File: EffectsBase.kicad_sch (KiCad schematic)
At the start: 17 parts, among them J1 PCIE_FX, J2 Conn_01x02, J3 Conn_01x02, K2 G6K-2, SW1 SW_DPDT_x2, SW2 SW_DPDT_x2, SW3 SW_DPDT_x2, SW4 SW_DPDT_x2, U1 STM32F103C8Tx, X1 PEDAL_COMBO_TOP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

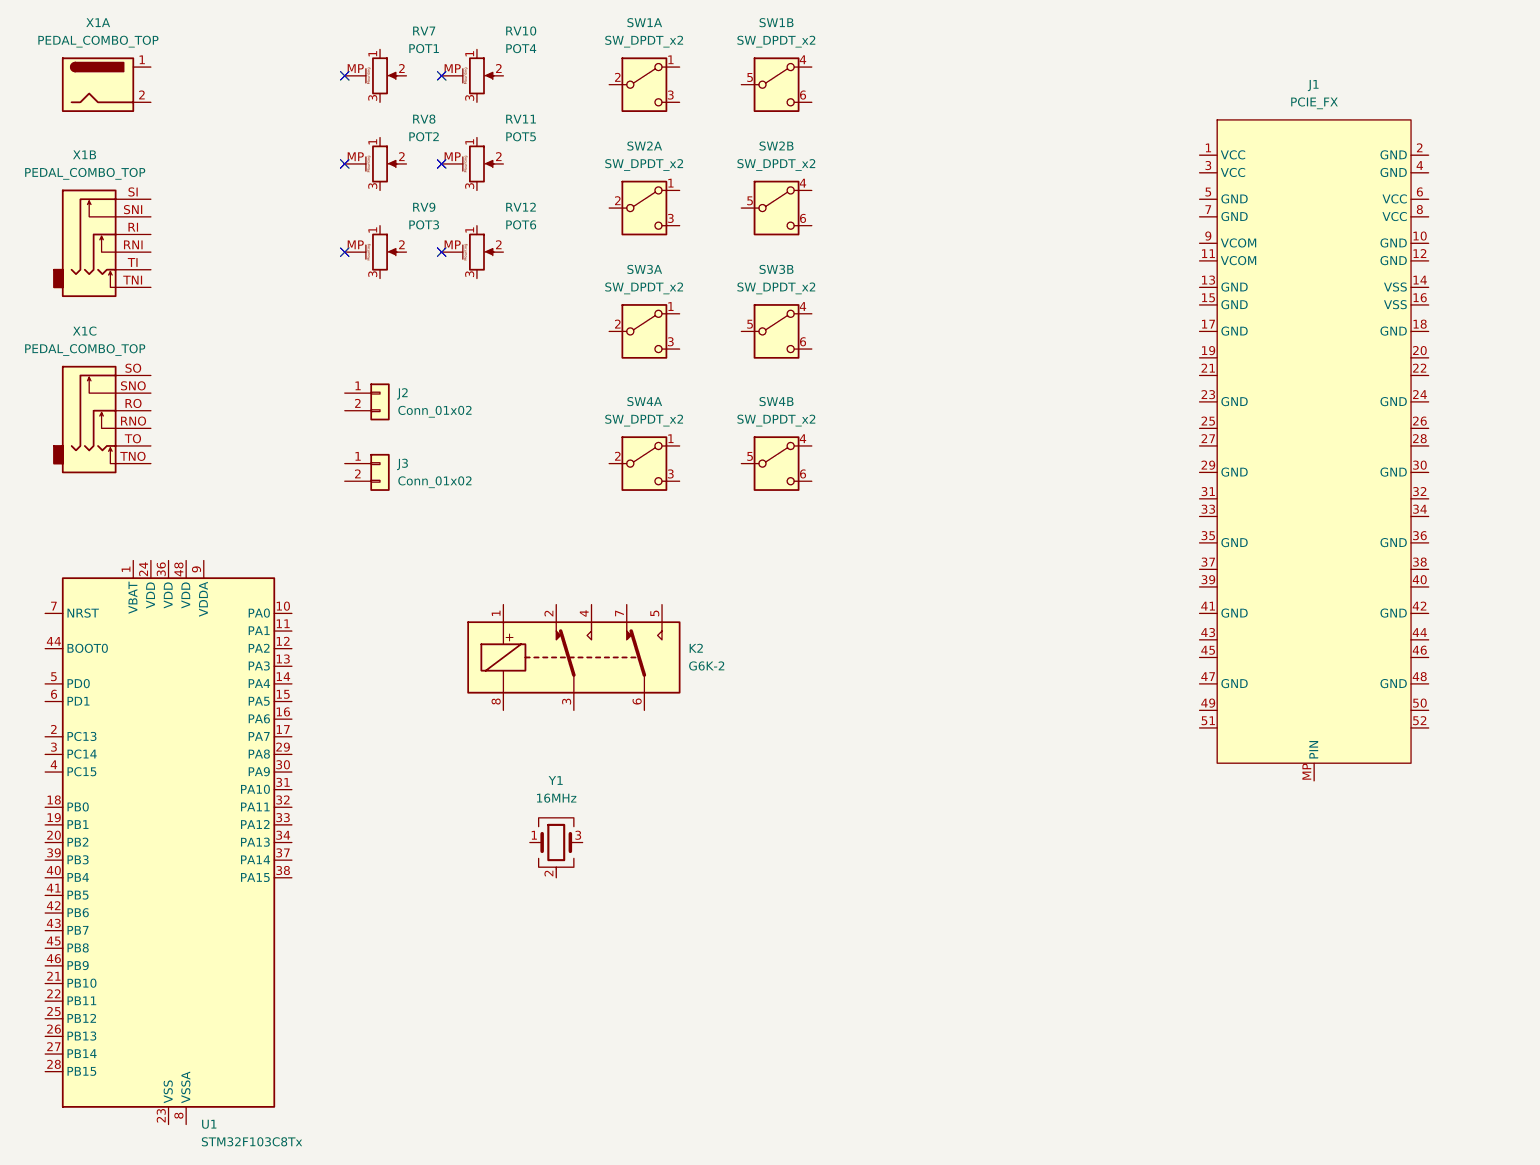
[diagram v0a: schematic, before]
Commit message: Initial schematic
Finished the base schematic.
Included all the controls and updated the power supply.
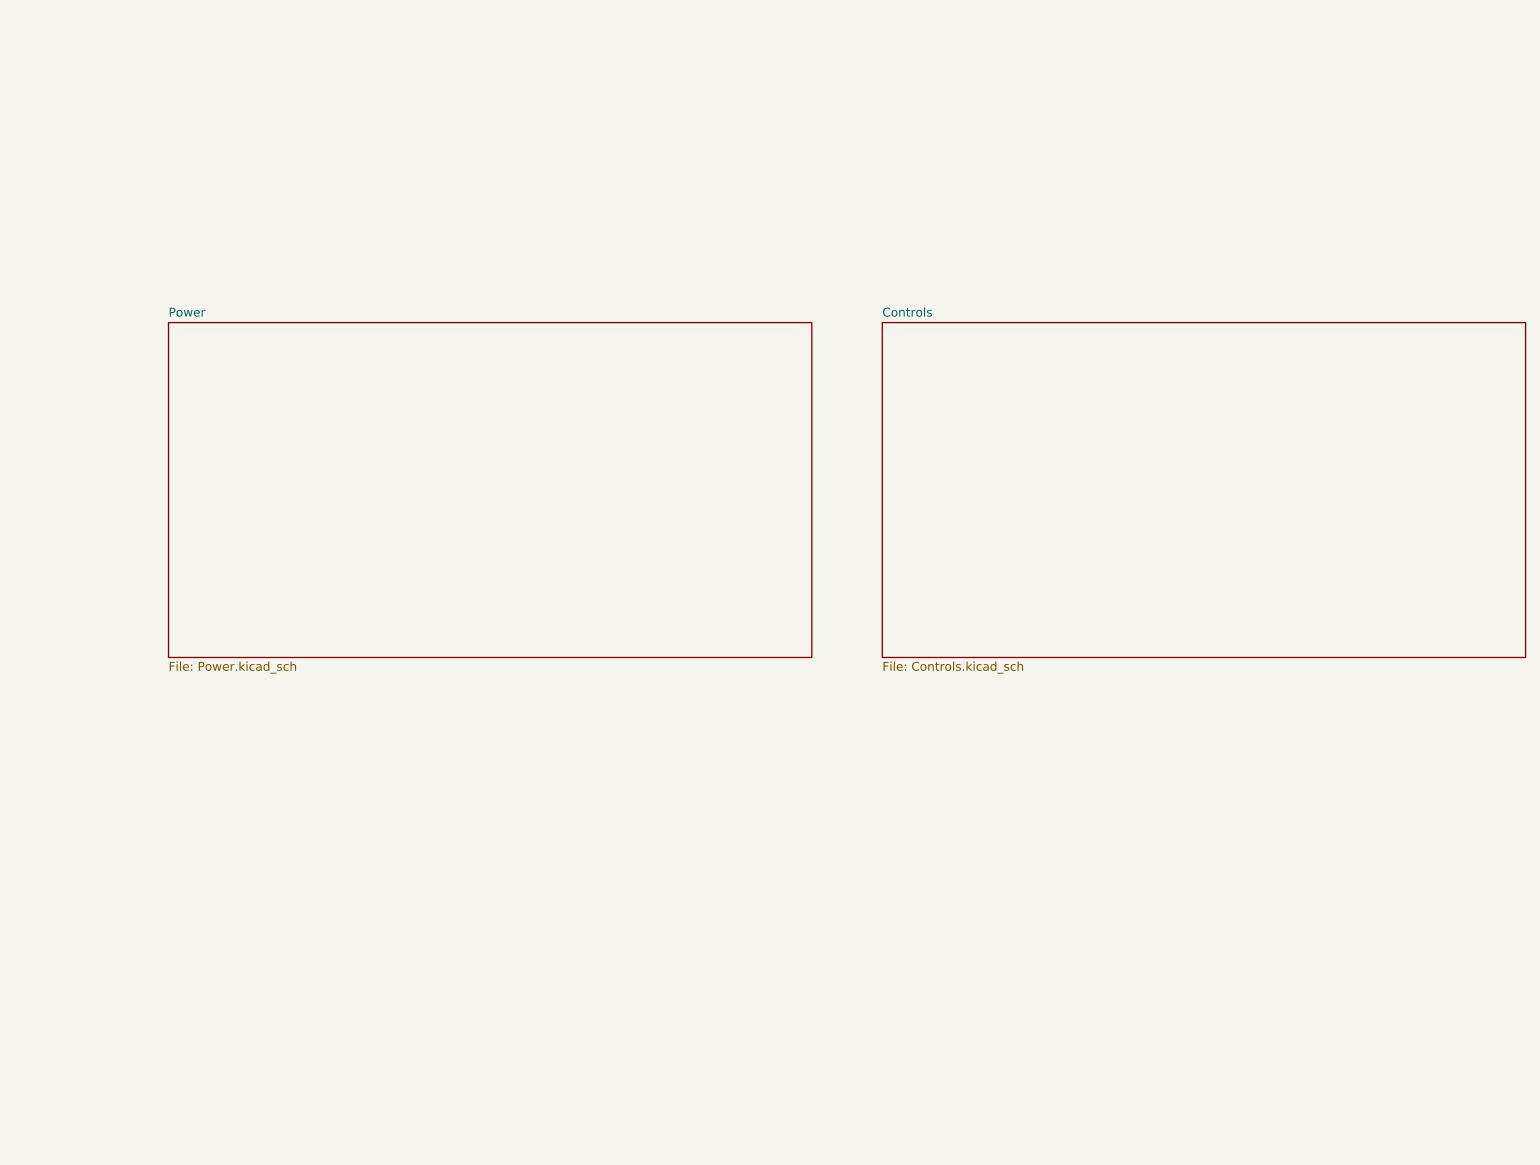
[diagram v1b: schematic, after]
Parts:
- removed J1: PCIE_FX, Custom_Parts:Mini PCI_Express, symbol Custom_Parts:PCIeFX
- removed J2, J3: Conn_01x02, Custom_Parts:JST_ZH_B2BZR_1x02_P1.50MM_VERTICAL, symbol Connector_Generic:Conn_01x02
- removed K2: G6K-2, Relay_SMD:Relay_DPDT_Omron_G6K-2F-Y, symbol Relay:G6K-2
- removed RV10: POT4, Custom_Parts:POT_SINGLE_VERTICAL_6X15, symbol Device:R_Potentiometer_MountingPin
- removed RV11: POT5, Custom_Parts:POT_SINGLE_VERTICAL_6X15, symbol Device:R_Potentiometer_MountingPin
- removed RV12: POT6, Custom_Parts:POT_SINGLE_VERTICAL_6X15, symbol Device:R_Potentiometer_MountingPin
- removed RV7: POT1, Custom_Parts:POT_SINGLE_VERTICAL_6X15, symbol Device:R_Potentiometer_MountingPin
- removed RV8: POT2, Custom_Parts:POT_SINGLE_VERTICAL_6X15, symbol Device:R_Potentiometer_MountingPin
- removed RV9: POT3, Custom_Parts:POT_SINGLE_VERTICAL_6X15, symbol Device:R_Potentiometer_MountingPin
- removed SW1, SW2, SW3, SW4: SW_DPDT_x2, Custom_Parts:SW_DPDT, symbol Switch:SW_DPDT_x2
- removed U1: STM32F103C8Tx, Package_QFP:LQFP-48_7x7mm_P0.5mm, symbol MCU_ST_STM32F1:STM32F103C8Tx
- removed X1: PEDAL_COMBO_TOP, Custom_Parts:PEDAL_COMBO_TOP, symbol Custom_Parts:PEDAL_COMBO_TOP
- removed Y1: 16MHz, Crystal:Crystal_SMD_3225-4Pin_3.2x2.5mm, symbol Device:Crystal_GND24
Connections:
- no-connect marks 6 -> 0
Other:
- added sheet Controls (Controls.kicad_sch)
- added sheet Power (Power.kicad_sch)
